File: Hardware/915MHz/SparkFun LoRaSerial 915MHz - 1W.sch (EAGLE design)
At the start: 58 parts, among them J1 QWIIC_RIGHT_ANGLE, J3 USB C, J4 JTAG, U2 ATSAMD21G-A, U3 AP2112K-3.3, U4 E19-915M30S, Y1 32.768kHz

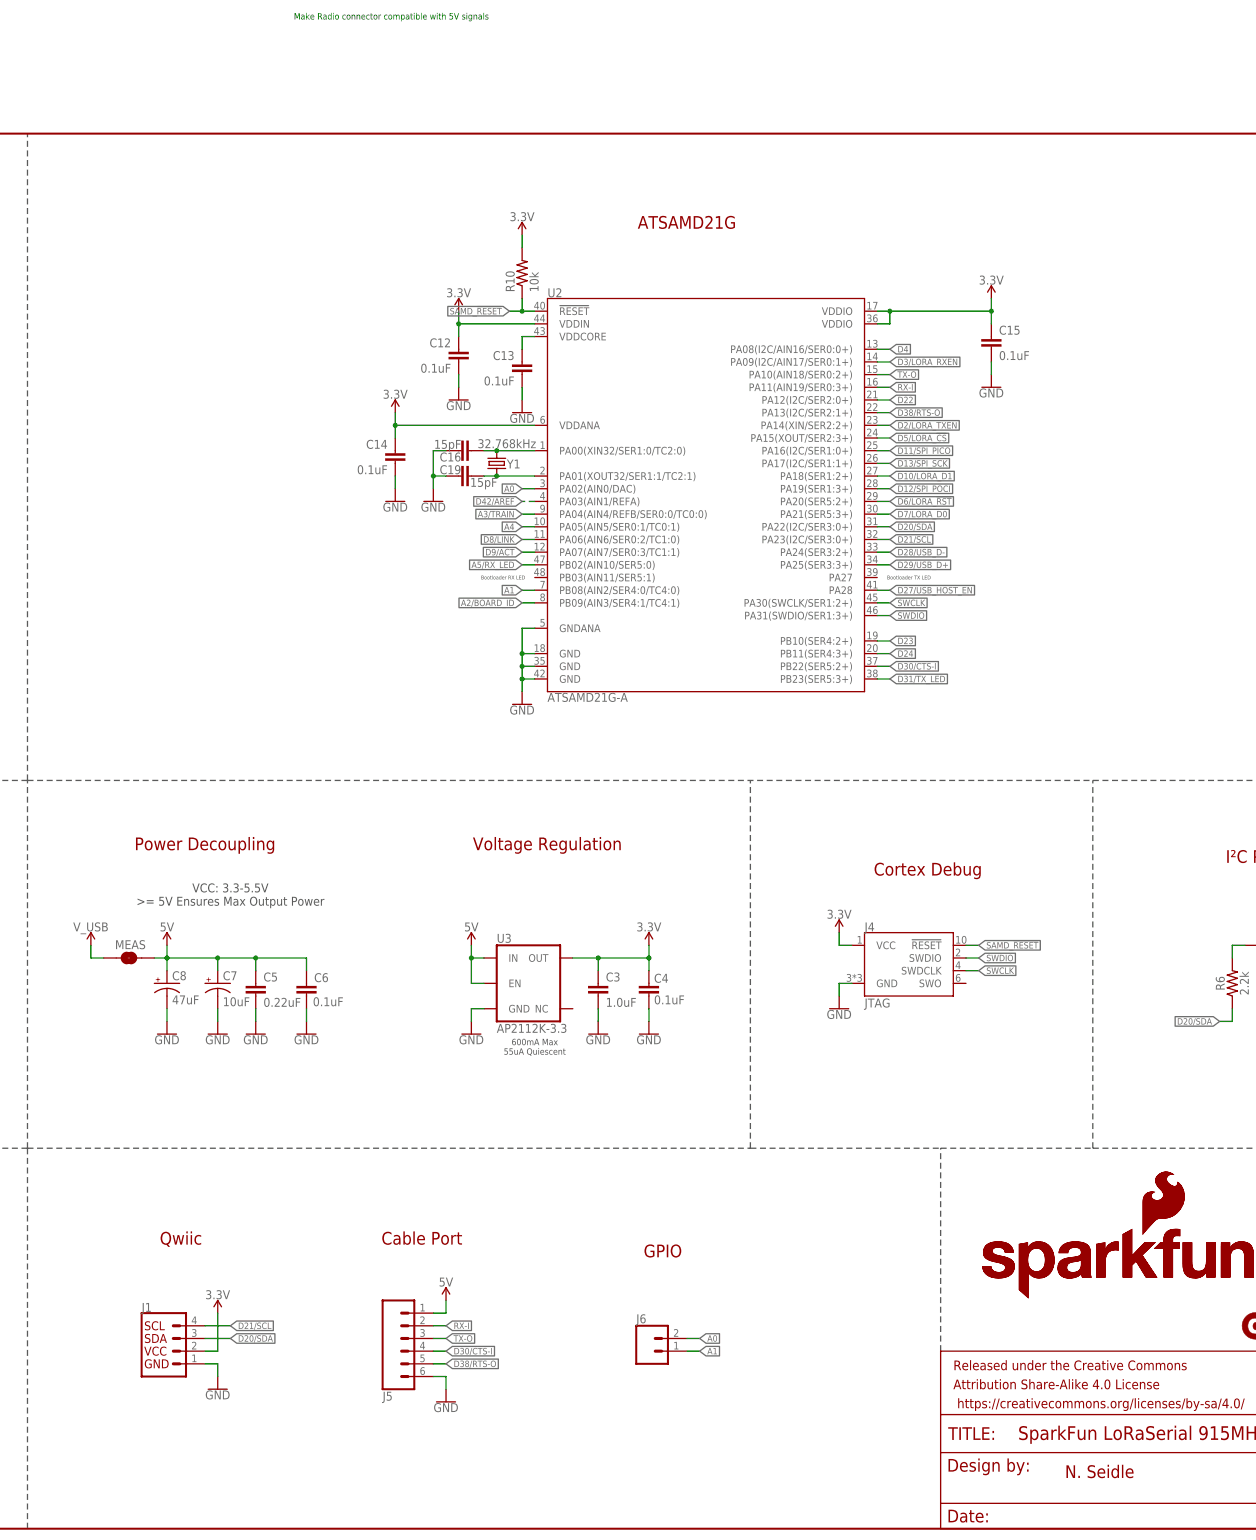
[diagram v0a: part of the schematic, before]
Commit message: Add sub folders for other frequencies
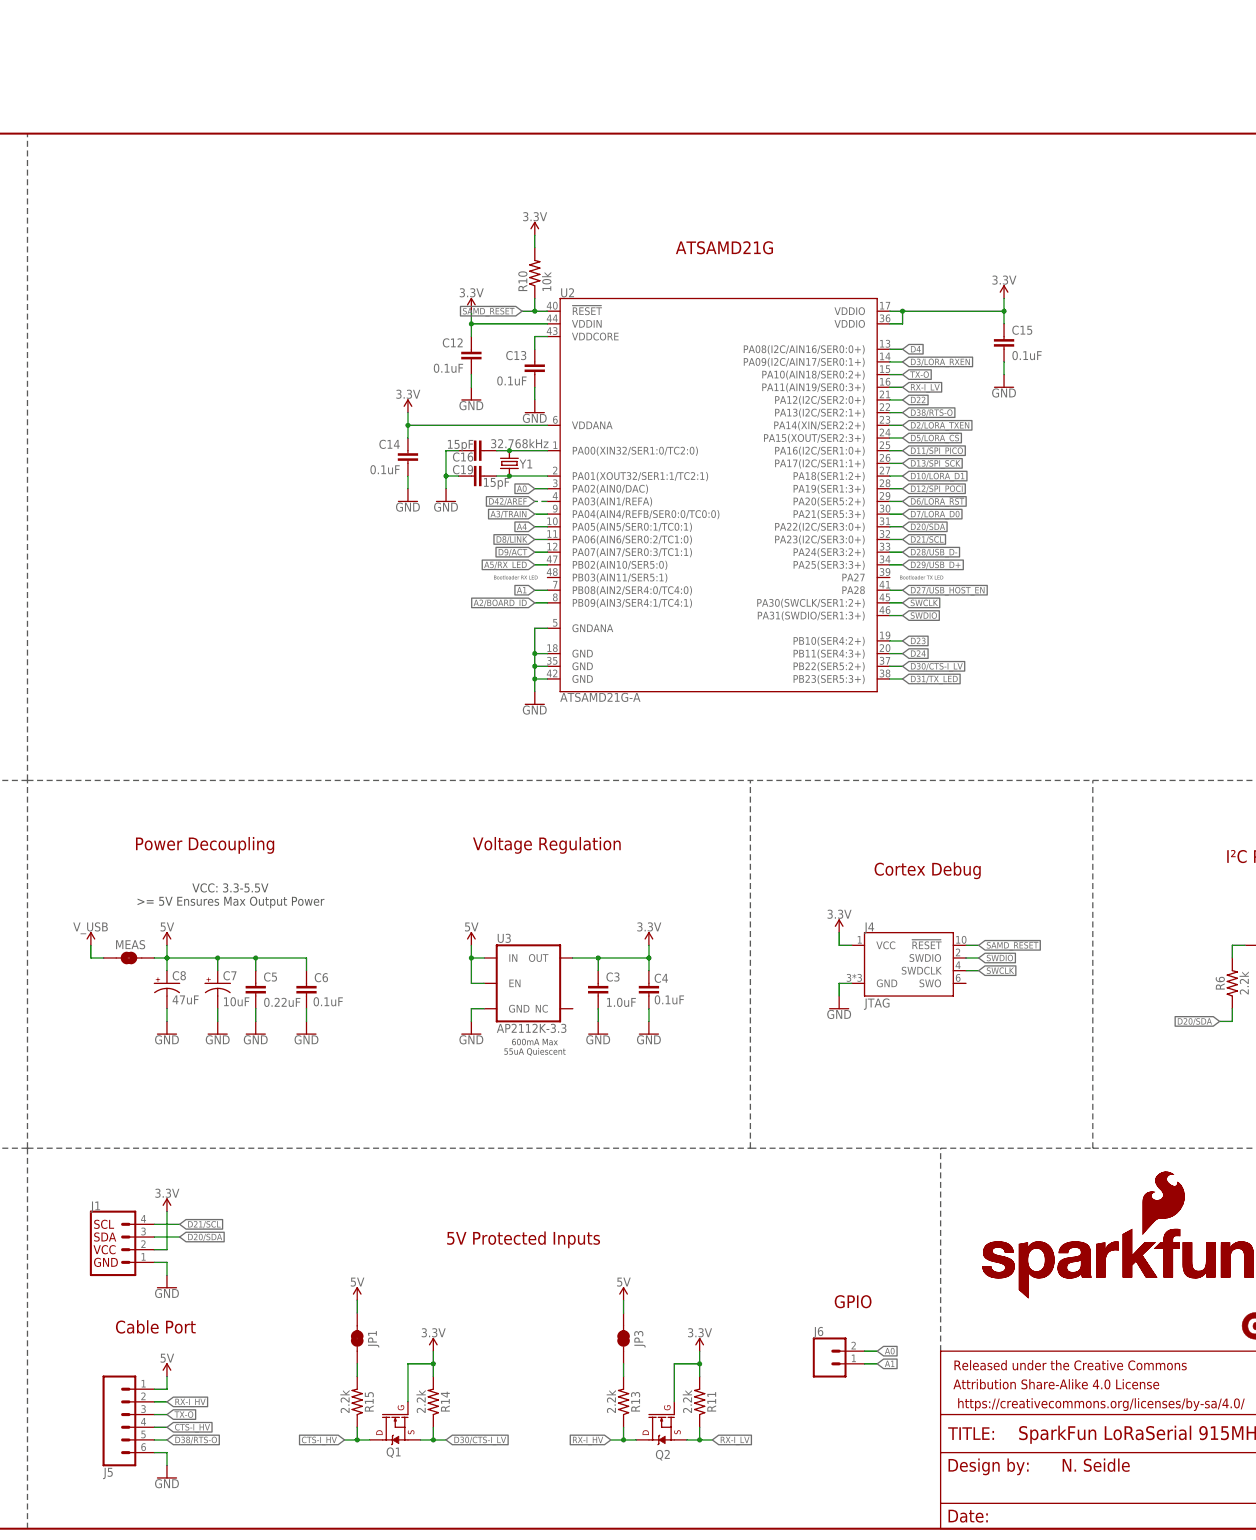
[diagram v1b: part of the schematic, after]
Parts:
- added JP1, JP3: JUMPER-SMT_2_NC_TRACE_SILK, SparkFun-Jumpers:JUMPER-SMT_2_NC_TRACE_SILK
- added Q1, Q2: 20V/0.2A/8MHz/1.2Ω/1Vth, SparkFun-DiscreteSemi:MOSFET-NCH-RE1C002UNTCL
- added R11, R13, R14, R15: 2.2k, SparkFun-Resistors:2.2KOHM-0603-1/10W-1%
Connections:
- removed net D30/CTS-I: J5.4, U2.PB22(SER5:2+)
- removed net RX-I: J5.2, U2.PA11(AIN19/SER0:3+)
- new net CTS-I_HV: J5.4, Q1.D, R15.1
- new net D30/CTS-I_LV: Q1.S, R14.1, U2.PB22(SER5:2+)
- new net N$5: JP3.1, R13.2
- new net N$6: JP1.1, R15.2
- new net RX-I_HV: J5.2, Q2.D, R13.1
- new net RX-I_LV: Q2.S, R11.1, U2.PA11(AIN19/SER0:3+)
- net 3.3V: now also Q1.G, Q2.G, R11.2, R14.2
- net 5V: now also JP1.2, JP3.2
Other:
- note added: "5V Protected Inputs"
- note removed: "Make Radio connector compatible with 5V signals"
- note removed: "Qwiic"
- moved on the sheet: C12, C13, C14, C15, C16, C19, J1, J5, J6, R10, U2, Y1

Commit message: Add RSSI LEDs
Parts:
- added D1, D7, D8: GREEN, SparkFun-LED:LED-GREEN0603
- added R20, R21, R22: 4.7k, SparkFun-Resistors:4.7KOHM-0603-1/10W-1%
- added U1: ESP32, SparkFun-RF:ESP32
- added U5: ESP-WROOM-3232D, SparkFun-RF:ESP-WROOM-3232D
- D2: value GREEN -> BLUE; device SparkFun-LED:LED-GREEN0603 -> SparkFun-LED:LED-BLUE0603
- D4: value BLUE -> GREEN; device SparkFun-LED:LED-BLUE0603 -> SparkFun-LED:LED-GREEN0603
- R5: value 4.7k -> 1k; device SparkFun-Resistors:4.7KOHM-0603-1/10W-1% -> SparkFun-Resistors:1KOHM-0603-1/10W-1%
- R9: value 1k -> 4.7k; device SparkFun-Resistors:1KOHM-0603-1/10W-1% -> SparkFun-Resistors:4.7KOHM-0603-1/10W-1%
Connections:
- removed net A3/TRAIN: S1.1, U2.PA04(AIN4/REFB/SER0:0/TC0:0)
- removed net A4: U2.PA05(AIN5/SER0:1/TC0:1)
- removed net D4: U2.PA08(I2C/AIN16/SER0:0+)
- removed net D8/LINK: D4.A, U2.PA06(AIN6/SER0:2/TC1:0)
- removed net D9/ACT: D5.A, U2.PA07(AIN7/SER0:3/TC1:1)
- new net A3/RSSI1: D1.A, U2.PA04(AIN4/REFB/SER0:0/TC0:0)
- new net A4/RSSI2: D4.A, U2.PA05(AIN5/SER0:1/TC0:1)
- new net D4/TRAIN: S1.1, U2.PA08(I2C/AIN16/SER0:0+)
- new net D8/RSSI3: D7.A, U2.PA06(AIN6/SER0:2/TC1:0)
- new net D9/RSSI4: D8.A, U2.PA07(AIN7/SER0:3/TC1:1)
- new net N$10: D7.C, R21.2
- new net N$11: D8.C, R22.2
- new net N$9: D1.C, R20.2
- net 3.3V: now also D5.A
- net GND: now also R20.1, R21.1, R22.1
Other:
- moved on the sheet: D2, D3, D4, D5, R1, R12, R2, R4, R5, R9, S1, S3

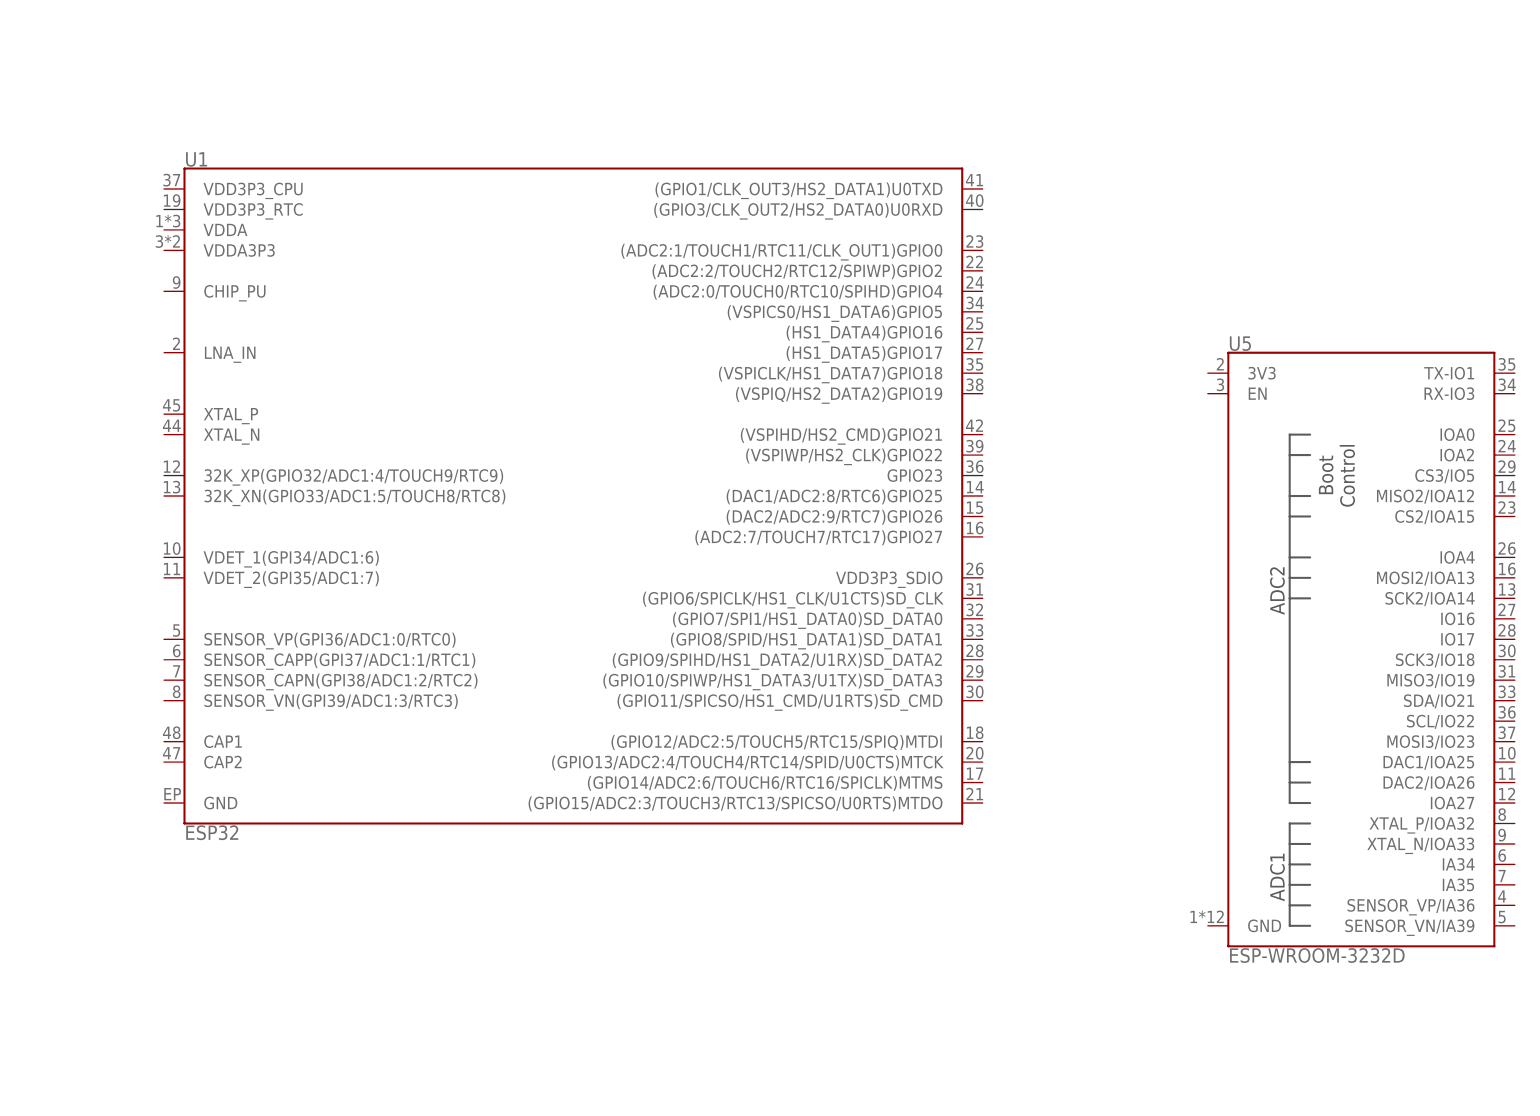
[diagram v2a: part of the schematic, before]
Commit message: Add RSSI LEDs
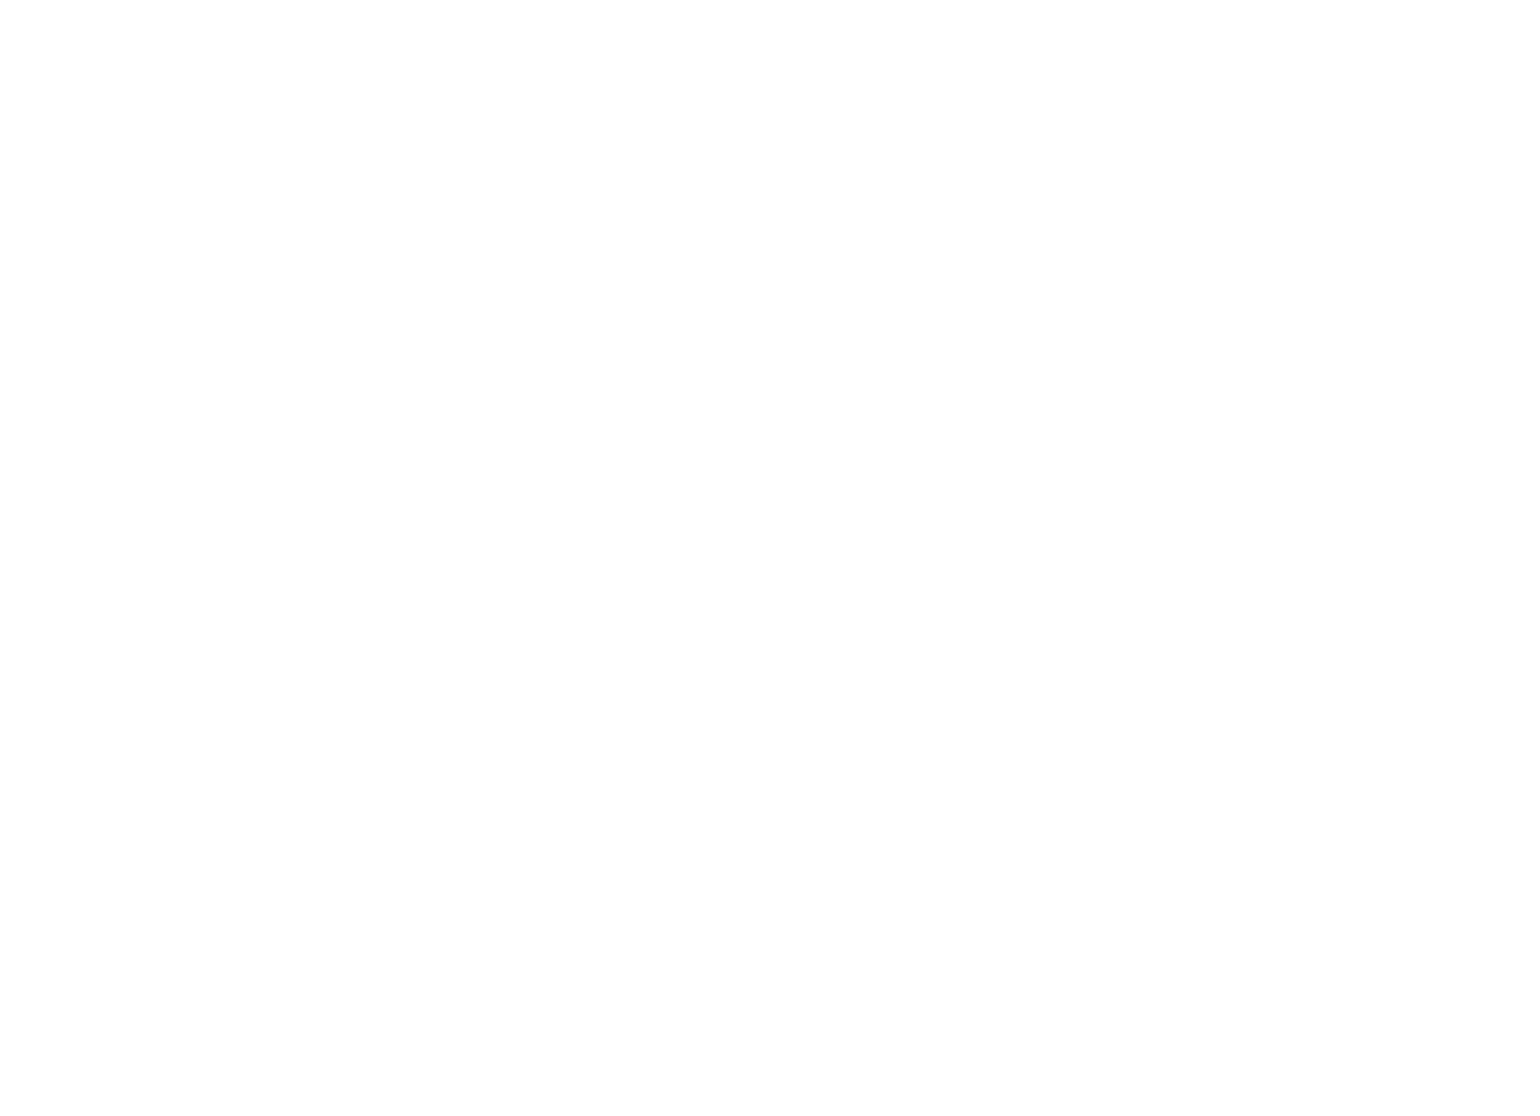
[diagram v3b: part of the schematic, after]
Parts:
- removed U1: ESP32, SparkFun-RF:ESP32
- removed U5: ESP-WROOM-3232D, SparkFun-RF:ESP-WROOM-3232D
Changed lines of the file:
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@@
 <part name="GND26" library="SparkFun-PowerSymbols" deviceset="GND" device=""/>
 <part name="SUPPLY18" library="SparkFun-PowerSymbols" deviceset="3.3V" device=""/>
-<part name="U1" library="SparkFun-RF" deviceset="ESP32" device=""/>
-<part name="U5" library="SparkFun-RF" deviceset="ESP-WROOM-32" device="32D"/>
 </parts>
 <sheets>
@@
 <attribute name="VALUE" x="60.96" y="119.634" size="1.778" layer="96" align="bottom-center"/>
 </instance>
-<instance part="U1" gate="G$1" x="535.94" y="200.66" smashed="yes">
-<attribute name="NAME" x="487.68" y="241.554" size="1.778" layer="95"/>
-<attribute name="VALUE" x="487.68" y="159.766" size="1.778" layer="96" align="top-left"/>
-</instance>
-<instance part="U5" gate="U1" x="635" y="180.34" smashed="yes">
-<attribute name="NAME" x="617.22" y="218.694" size="1.778" layer="95"/>
-<attribute name="VALUE" x="617.22" y="144.526" size="1.778" layer="96" align="top-left"/>
-</instance>
 </instances>
 <busses>
@@
 <net name="A2/BOARD_ID" class="0">
 <segment>
+<pinref part="U2" gate="G$1" pin="PB09(AIN3/SER4:1/TC4:1)"/>
+<wire x1="251.46" y1="185.42" x2="248.92" y2="185.42" width="0.1524" layer="91"/>
+<label x="248.92" y="185.42" size="1.27" layer="95" rot="R180" xref="yes"/>
+</segment>
+<segment>
 <pinref part="R2" gate="G$1" pin="1"/>
 <pinref part="R4" gate="G$1" pin="2"/>
@@
 <junction x="30.48" y="106.68"/>
 <label x="27.94" y="106.68" size="1.27" layer="95" rot="R180" xref="yes"/>
-</segment>
-<segment>
-<pinref part="U2" gate="G$1" pin="PB09(AIN3/SER4:1/TC4:1)"/>
-<wire x1="251.46" y1="185.42" x2="248.92" y2="185.42" width="0.1524" layer="91"/>
-<label x="248.92" y="185.42" size="1.27" layer="95" rot="R180" xref="yes"/>
 </segment>
 </net>
@@
 </segment>
 </net>
+<net name="D9/RSSI4" class="0">
+<segment>
+<pinref part="U2" gate="G$1" pin="PA07(AIN7/SER0:3/TC1:1)"/>
+<wire x1="251.46" y1="195.58" x2="248.92" y2="195.58" width="0.1524" layer="91"/>
+<label x="248.92" y="195.58" size="1.27" layer="95" rot="R180" xref="yes"/>
+</segment>
+<segment>
+<pinref part="D8" gate="G$1" pin="A"/>
+<wire x1="121.92" y1="114.3" x2="121.92" y2="116.84" width="0.1524" layer="91"/>
+<label x="121.92" y="116.84" size="1.27" layer="95" rot="R90" xref="yes"/>
+</segment>
+</net>
+<net name="D8/RSSI3" class="0">
+<segment>
+<pinref part="U2" gate="G$1" pin="PA06(AIN6/SER0:2/TC1:0)"/>
+<wire x1="251.46" y1="198.12" x2="248.92" y2="198.12" width="0.1524" layer="91"/>
+<label x="248.92" y="198.12" size="1.27" layer="95" rot="R180" xref="yes"/>
+</segment>
+<segment>
+<pinref part="D7" gate="G$1" pin="A"/>
+<wire x1="111.76" y1="114.3" x2="111.76" y2="116.84" width="0.1524" layer="91"/>
+<label x="111.76" y="116.84" size="1.27" layer="95" rot="R90" xref="yes"/>
+</segment>
+</net>
+<net name="A4/RSSI2" class="0">
+<segment>
+<pinref part="U2" gate="G$1" pin="PA05(AIN5/SER0:1/TC0:1)"/>
+<wire x1="251.46" y1="200.66" x2="248.92" y2="200.66" width="0.1524" layer="91"/>
+<label x="248.92" y="200.66" size="1.27" layer="95" rot="R180" xref="yes"/>
+</segment>
+<segment>
+<pinref part="D4" gate="G$1" pin="A"/>
+<wire x1="101.6" y1="114.3" x2="101.6" y2="116.84" width="0.1524" layer="91"/>
+<label x="101.6" y="116.84" size="1.27" layer="95" rot="R90" xref="yes"/>
+</segment>
+</net>
 <net name="D4/TRAIN" class="0">
+<segment>
+<pinref part="U2" gate="G$1" pin="PA08(I2C/AIN16/SER0:0+)"/>
+<wire x1="320.04" y1="236.22" x2="322.58" y2="236.22" width="0.1524" layer="91"/>
+<label x="322.58" y="236.22" size="1.27" layer="95" xref="yes"/>
+</segment>
 <segment>
 <pinref part="S1" gate="G$1" pin="1"/>
@@
 <label x="40.64" y="106.68" size="1.27" layer="95" rot="R90" xref="yes"/>
 </segment>
-<segment>
-<pinref part="U2" gate="G$1" pin="PA08(I2C/AIN16/SER0:0+)"/>
-<wire x1="320.04" y1="236.22" x2="322.58" y2="236.22" width="0.1524" layer="91"/>
-<label x="322.58" y="236.22" size="1.27" layer="95" xref="yes"/>
-</segment>
-</net>
-<net name="D9/RSSI4" class="0">
-<segment>
-<pinref part="U2" gate="G$1" pin="PA07(AIN7/SER0:3/TC1:1)"/>
-<wire x1="251.46" y1="195.58" x2="248.92" y2="195.58" width="0.1524" layer="91"/>
-<label x="248.92" y="195.58" size="1.27" layer="95" rot="R180" xref="yes"/>
-</segment>
-<segment>
-<pinref part="D8" gate="G$1" pin="A"/>
-<wire x1="121.92" y1="114.3" x2="121.92" y2="116.84" width="0.1524" layer="91"/>
-<label x="121.92" y="116.84" size="1.27" layer="95" rot="R90" xref="yes"/>
-</segment>
-</net>
-<net name="D8/RSSI3" class="0">
-<segment>
-<pinref part="U2" gate="G$1" pin="PA06(AIN6/SER0:2/TC1:0)"/>
-<wire x1="251.46" y1="198.12" x2="248.92" y2="198.12" width="0.1524" layer="91"/>
-<label x="248.92" y="198.12" size="1.27" layer="95" rot="R180" xref="yes"/>
-</segment>
-<segment>
-<pinref part="D7" gate="G$1" pin="A"/>
-<wire x1="111.76" y1="114.3" x2="111.76" y2="116.84" width="0.1524" layer="91"/>
-<label x="111.76" y="116.84" size="1.27" layer="95" rot="R90" xref="yes"/>
-</segment>
-</net>
-<net name="A4/RSSI2" class="0">
-<segment>
-<pinref part="U2" gate="G$1" pin="PA05(AIN5/SER0:1/TC0:1)"/>
-<wire x1="251.46" y1="200.66" x2="248.92" y2="200.66" width="0.1524" layer="91"/>
-<label x="248.92" y="200.66" size="1.27" layer="95" rot="R180" xref="yes"/>
-</segment>
-<segment>
-<pinref part="D4" gate="G$1" pin="A"/>
-<wire x1="101.6" y1="114.3" x2="101.6" y2="116.84" width="0.1524" layer="91"/>
-<label x="101.6" y="116.84" size="1.27" layer="95" rot="R90" xref="yes"/>
-</segment>
-</net>
+</net>
